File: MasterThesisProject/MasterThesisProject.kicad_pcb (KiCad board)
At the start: 2 copper layers, 94.5 x 97 mm, 45 parts, among them J2 Barrel_Jack, SW1 SW_MEC_5E, U1 LCD_I2C, U10 TGS5342, U11 CDM7160, U12 INA128, U13 LM4041AILT-1.2, U14 LPS331PA_Module, U15 W5500_SPI_ETH, U2 SensironSPS30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

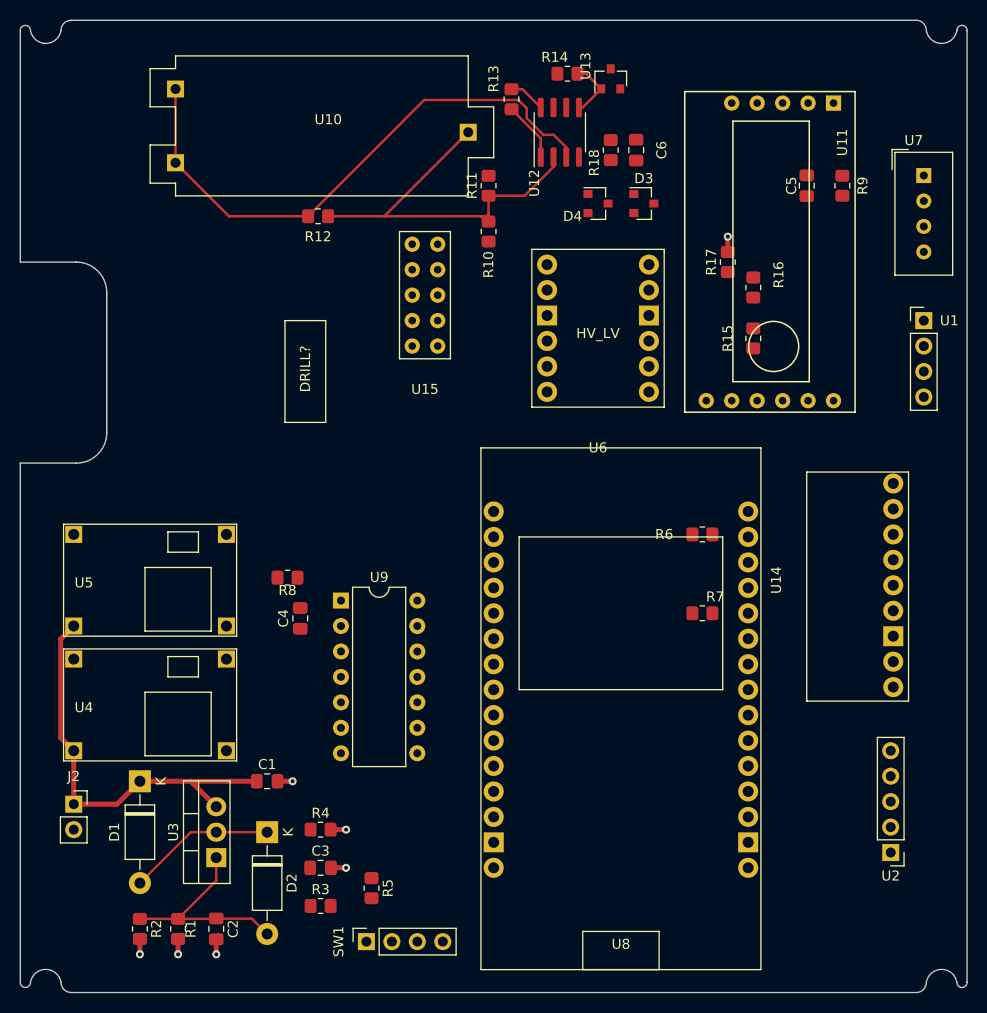
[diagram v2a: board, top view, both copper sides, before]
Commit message: Add all paths, copper layers etc
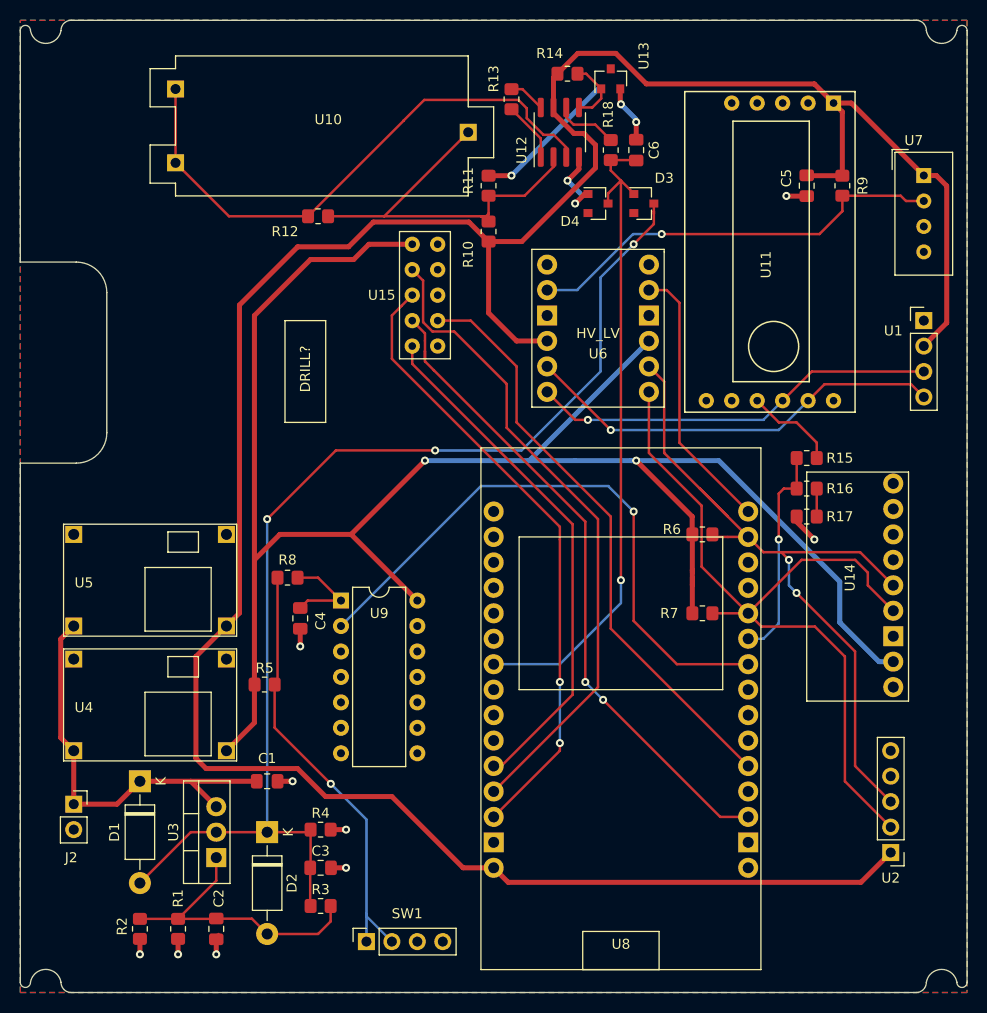
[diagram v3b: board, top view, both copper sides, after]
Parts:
- moved R17 26.6 mm to (249.2, 84.8), turned to 180 degrees
- moved R5 23.0 mm to (195.1, 101.6), turned to 0 degrees
- moved R16 20.8 mm to (249.2, 82.0), turned to 0 degrees
- moved R15 13.1 mm to (249.2, 79.0), turned to 180 degrees
- turned C4 to 270 degrees
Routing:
- net +5V: track 0.00 -> 264.8 mm
- net +3V3: track 0.00 -> 187.1 mm, vias 0 -> 2
- net +3V0: track 15.2 -> 117.1 mm, vias 0 -> 3
- net SDA: track 0.00 -> 79.7 mm
- net SCL: track 0.00 -> 74.6 mm, vias 0 -> 2
- net CO_SENSOR: track 0.00 -> 67.1 mm, vias 0 -> 1
- net SPI_CS: track 0.00 -> 65.9 mm, vias 0 -> 2
- net SPI_MISO: track 0.00 -> 65.3 mm
- net SPI_MOSI: track 0.00 -> 62.6 mm, vias 0 -> 2
- net LCD_BUTTON: track 0.00 -> 60.2 mm, vias 0 -> 1
- net ETH_INT: track 0.00 -> 59.2 mm
- net SPI_CLK: track 0.00 -> 52.2 mm
- net Net-(R5-Pad2): track 0.00 -> 44.1 mm, vias 0 -> 1
- net SCL_HIGH: track 0.00 -> 42.6 mm, vias 0 -> 1
- net DHT_HIGH: track 0.00 -> 42.6 mm, vias 0 -> 1
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- added copper zone on B.Cu, net GND
- added copper zone on F.Cu, net GND

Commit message: Add signature to PCB, generate gerber files
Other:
- board text added: "Lukasz Kania"
- board text added: "Master Thesis 2021"
